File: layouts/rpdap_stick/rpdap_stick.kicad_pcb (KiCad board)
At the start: 4 copper layers, 66 x 43.2 mm, 69 parts

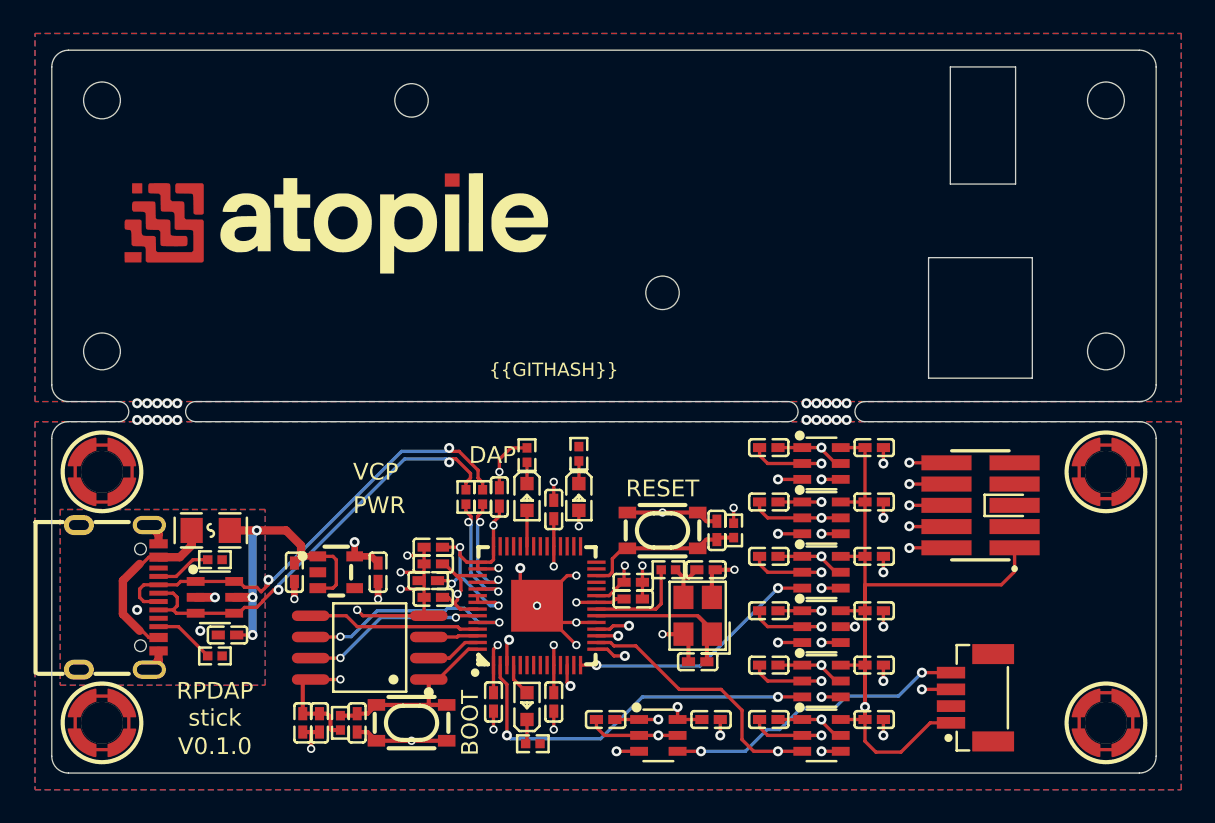
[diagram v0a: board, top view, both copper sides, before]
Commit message: rebuild with upstream rp2040 fixes. move header .25mm to the right. center dap-LED
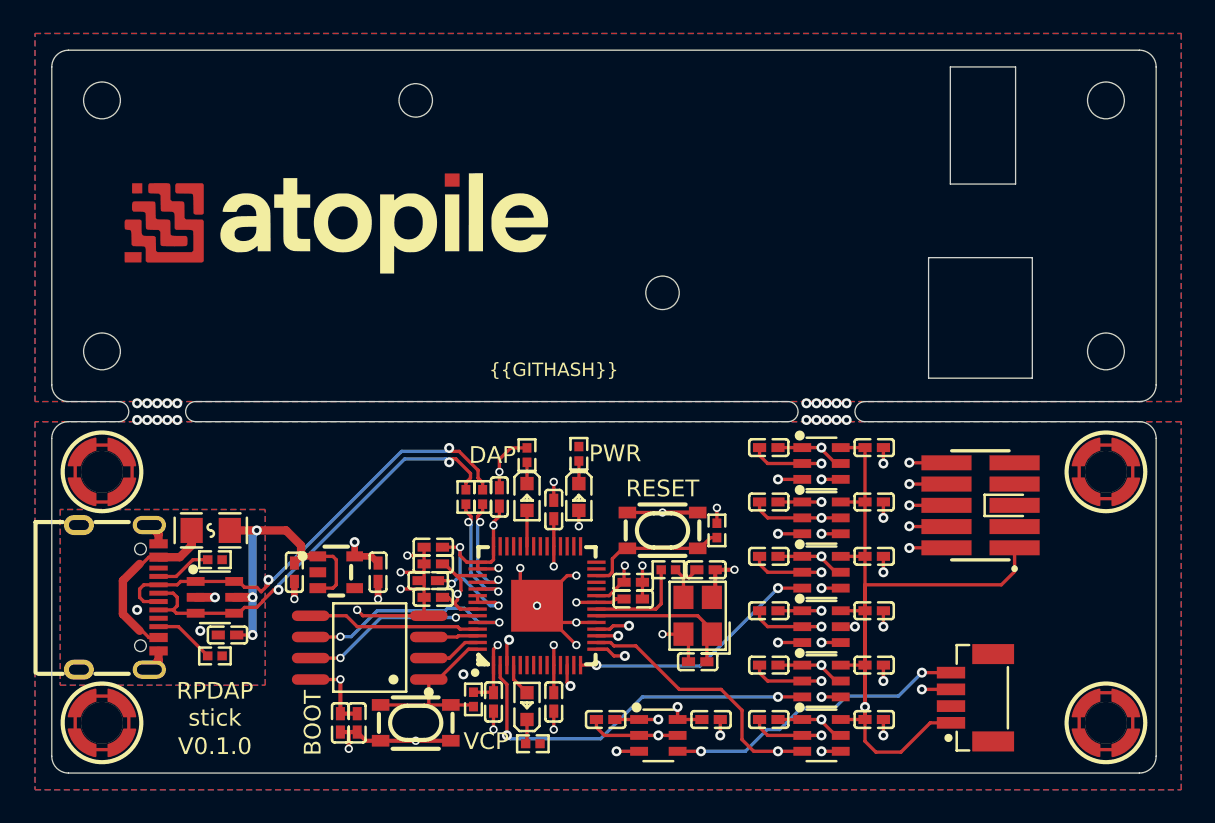
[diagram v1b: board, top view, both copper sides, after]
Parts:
- removed C15, C30: 1µF ±10% 25V X5R, Samsung_Electro_Mechanics_CL05A105KA5NQNC:C0402
- X1: footprint Yangxing_Tech_X322512MSB4SI:CRYSTAL-SMD_4P-L3.2-W2.5-BL -> Abracon_LLC_ABM8_272_T3:CRYSTAL-SMD_4P-L3.2-W2.5-BL
- moved R2 8.07 mm to (25.2, 17.2)
- moved C29 2.25 mm to (18.3, 18.6)
- moved C28 2.25 mm to (17.2, 18.6)
- moved R5 1.00 mm to (39.7, 7.10), turned to 90 degrees
- moved SW1 0.25 mm to (21.8, 18.6), turned to 0 degrees
- turned SW2 to 180 degrees
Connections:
- net RP_USB_N renamed output-USB_D_N
- net RP_USB_P renamed output-USB_D_P
- net USB_N renamed input-USB_D_N
- net USB_P renamed input-USB_D_P
- net anode renamed power-anode
- C11 pad 1: 3V3 -> _power_3v3-anode
- C13 pad 1: 3V3 -> _power_3v3-anode
- C2 pad 1: 3V3 -> _power_3v3-anode
- C21 pad 1: 3V3 -> _power_3v3-anode
- C22 pad 1: 3V3 -> _power_3v3-anode
- C23 pad 1: 3V3 -> _power_3v3-anode
- C24 pad 1: 3V3 -> _power_3v3-anode
- C25 pad 1: 3V3 -> _power_3v3-anode
- C26 pad 1: 3V3 -> _power_3v3-anode
- C27 pad 1: 3V3 -> _power_3v3-anode
- C28 pad 1: 3V3 -> _power_3v3-anode
- C29 pad 1: 3V3 -> _power_3v3-anode
- C3 pad 1: 3V3 -> _power_3v3-anode
- C32 pad 1: 3V3 -> _power_3v3-anode
- C5 pad 1: 3V3 -> _power_3v3-anode
- C7 pad 1: 3V3 -> _power_3v3-anode
- C9 pad 1: 3V3 -> _power_3v3-anode
- LED2 pad 2: 3V3 -> _power_3v3-anode
- R2 pad 1: 3V3 -> chip_select
- R2 pad 2: chip_select -> _power_3v3-anode
- R5 pad 1: 3V3 -> RUN
- R5 pad 2: RUN -> _power_3v3-anode
- SW1 pad 1: GND -> chip_select
- SW1 pad 2: GND -> chip_select
- SW1 pad 3: chip_select -> GND
- SW1 pad 4: chip_select -> GND
- SW2 pad 1: GND -> RUN
- SW2 pad 2: GND -> RUN
- SW2 pad 3: RUN -> GND
- SW2 pad 4: RUN -> GND
- U1 pad 5: 3V3 -> _power_3v3-anode
- U15 pad 1: 3V3 -> _power_3v3-anode
- U2 pad 1: 3V3 -> _power_3v3-anode
- U3 pad 1: 3V3 -> _power_3v3-anode
- U3 pad 5: 3V3 -> _power_3v3-anode
- U4 pad 1: 3V3 -> _power_3v3-anode
- U5 pad 1: 3V3 -> _power_3v3-anode
- U5 pad 5: 3V3 -> _power_3v3-anode
- U6 pad 1: 3V3 -> _power_3v3-anode
- U6 pad 5: 3V3 -> _power_3v3-anode
- U7 pad 1: 3V3 -> _power_3v3-anode
- U7 pad 5: 3V3 -> _power_3v3-anode
- U8 pad 1: 3V3 -> _power_3v3-anode
- U8 pad 10: 3V3 -> _power_3v3-anode
- U8 pad 22: 3V3 -> _power_3v3-anode
- U8 pad 33: 3V3 -> _power_3v3-anode
- U8 pad 42: 3V3 -> _power_3v3-anode
- U8 pad 43: 3V3 -> _power_3v3-anode
- U8 pad 44: 3V3 -> _power_3v3-anode
- U8 pad 48: 3V3 -> _power_3v3-anode
- U8 pad 49: 3V3 -> _power_3v3-anode
- U9 pad 8: 3V3 -> _power_3v3-anode
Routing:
- net GND: track 142.8 -> 0.00 mm, vias 36 -> 0
- net (no net): track 0.00 -> 141.7 mm, vias 22 -> 59
- net 3V3: track 64.7 -> 0.00 mm, vias 20 -> 0
- net _power_3v3-anode: track 0.00 -> 63.9 mm, vias 0 -> 20
- net chip_select: track 12.9 -> 10.8 mm
- net RUN: track 9.61 -> 8.61 mm
- added copper zone on In1.Cu, net _power_3v3-anode
- removed copper zone on In1.Cu, net 3V3
- removed copper zone on B.Cu, net GND
- removed copper zone on F.Cu, net GND
- removed copper zone on In2.Cu, net GND
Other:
- outline, holes or cut-outs redrawn
- board text added: "V0.1.1"
